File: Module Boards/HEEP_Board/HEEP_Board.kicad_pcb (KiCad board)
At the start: 6 copper layers, 17.5 x 26.4 mm, 46 parts, among them U2 HEEPocrates, U3 SIT1532AC-J5-DCC-32.768D, U4 W25Q128JWYIQ

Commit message: Fixed path dependencies and changed library name to X-MODs
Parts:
- C1, C10, C11, C12, C13, C14, C15, C16, C17, C18, C2, C3, C4, C5, C6, C7, C8, C9: footprint HeepoMind_PcbLib:C0402 -> X-MODs_PcbLib:C0402
- J1: footprint HeepoMind_PcbLib:HEEP_Board_Castellated_Conn_1.27mm -> X-MODs_PcbLib:HEEP_Board_Castellated_Conn_1.27mm
- R1, R2, R3, R4, R5, R6, R7, R8, R9: footprint HeepoMind_PcbLib:R0402 -> X-MODs_PcbLib:R0402
- SW1: footprint HeepoMind_PcbLib:TL1030AF160AQJ -> X-MODs_PcbLib:TL1030AF160AQJ
- U1, U7: footprint HeepoMind_PcbLib:X2SON-6 -> X-MODs_PcbLib:X2SON-6
- U2: footprint HeepoMind_PcbLib:HEEPocrates -> X-MODs_PcbLib:HEEPocrates
- U3: footprint HeepoMind_PcbLib:SIT1532AC -> X-MODs_PcbLib:SIT1532AC
- U4: footprint HeepoMind_PcbLib:WLCSP-21 -> X-MODs_PcbLib:WLCSP-21
- U5, U6: footprint HeepoMind_PcbLib:X2SON-8 -> X-MODs_PcbLib:X2SON-8

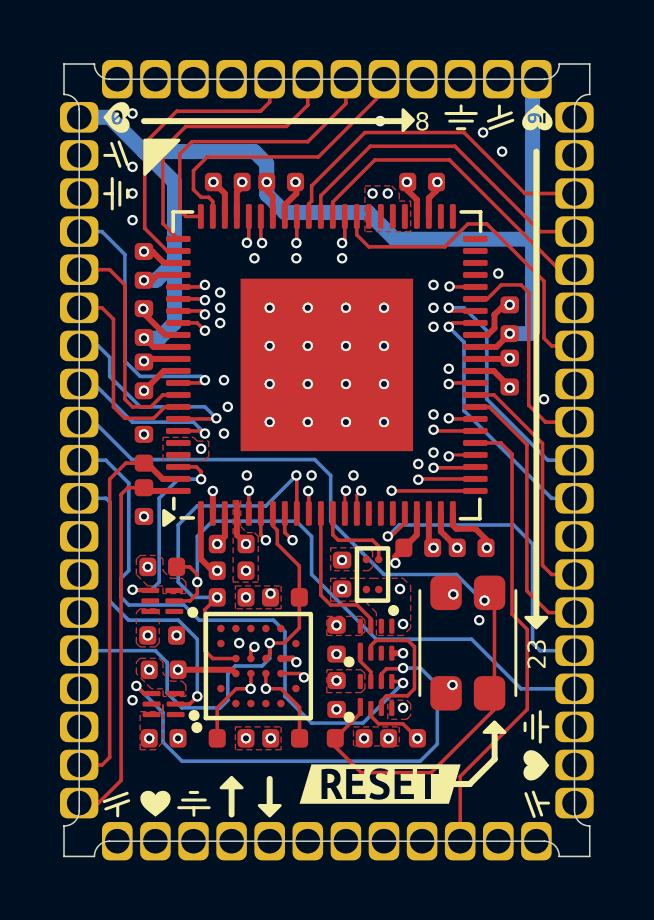
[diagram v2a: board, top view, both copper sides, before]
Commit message: Added ADC to board and partially placed/routed the updated board
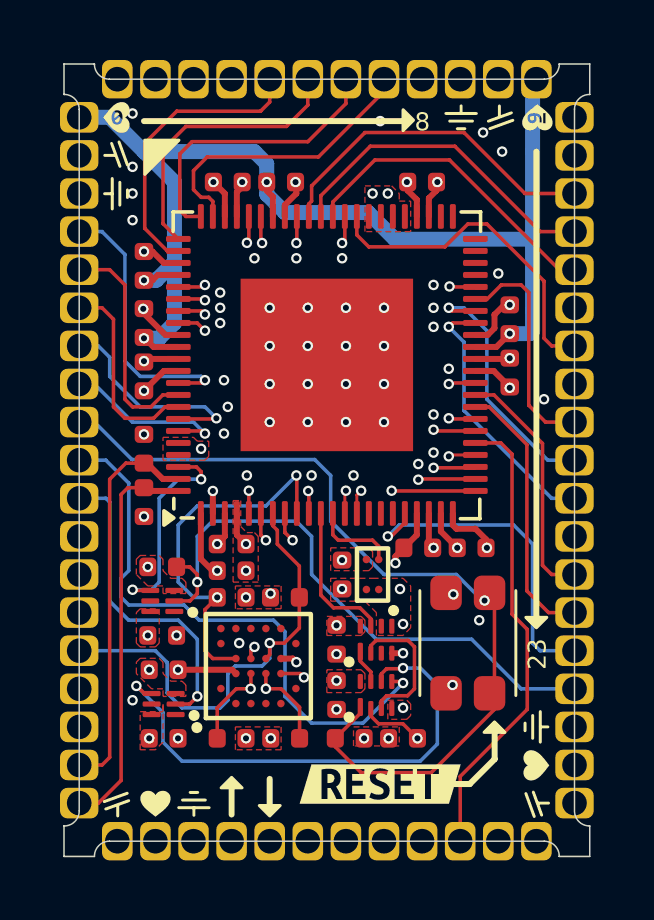
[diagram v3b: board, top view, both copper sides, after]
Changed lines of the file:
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@@
-	)
-	(segment
-		(start 107.696 108.966)
-		(end 107.369 108.639)
-		(width 0.12)
-		(layer "F.Cu")
-		(net 52)
-	)
-	(segment
-		(start 109.0345 109.4235)
-		(end 108.577 108.966)
-		(width 0.12)
-		(layer "F.Cu")
-		(net 52)
 	)
 	(segment
@@
 	)
 	(segment
-		(start 108.577 108.966)
-		(end 107.696 108.966)
+		(start 107.79 109.06)
+		(end 107.369 108.639)
+		(width 0.12)
+		(layer "F.Cu")
+		(net 52)
+	)
+	(segment
+		(start 108.671 109.06)
+		(end 107.79 109.06)
 		(width 0.12)
 		(layer "F.Cu")
@@
 		(width 0.12)
 		(layer "F.Cu")
+		(net 52)
+	)
+	(segment
+		(start 109.0345 109.4235)
+		(end 108.671 109.06)
+		(width 0.12)
+		(layer "F.Cu")
